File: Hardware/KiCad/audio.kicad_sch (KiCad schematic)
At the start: 36 parts, among them IC1 LM4861M, J4 Kenwood-3.5, J5 Kenwood-2.5, SW1 PTT, U5 MAX9814

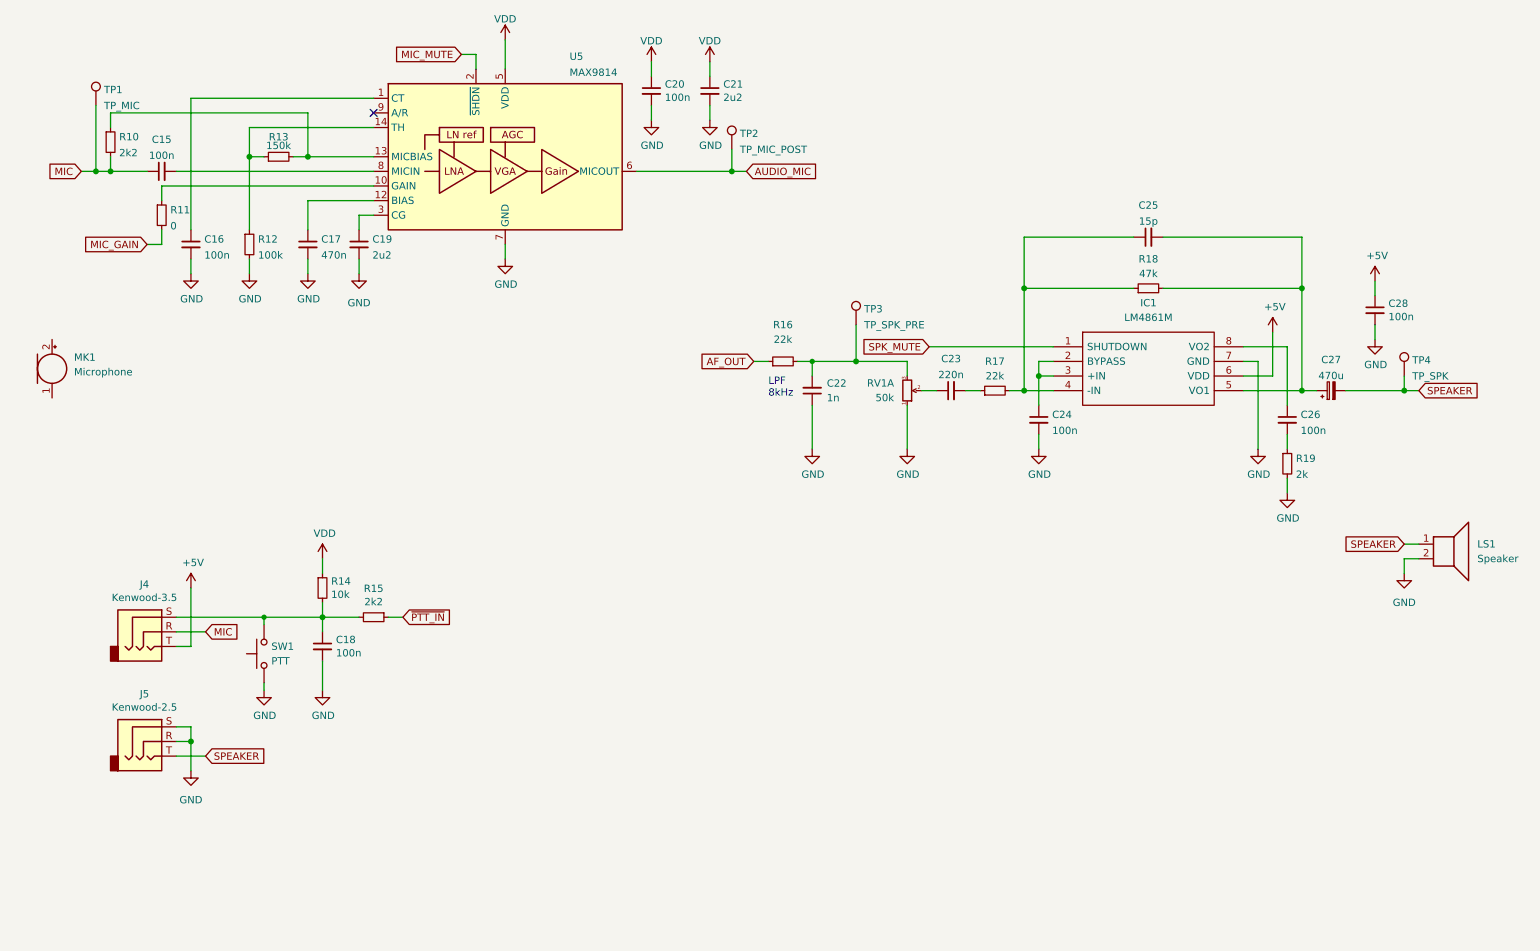
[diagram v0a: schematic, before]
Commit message: fixup PTT/Audio (Issue 14), add RGB LED (Issue 26), Connect LEDs to MCU & add them to the .ioc file
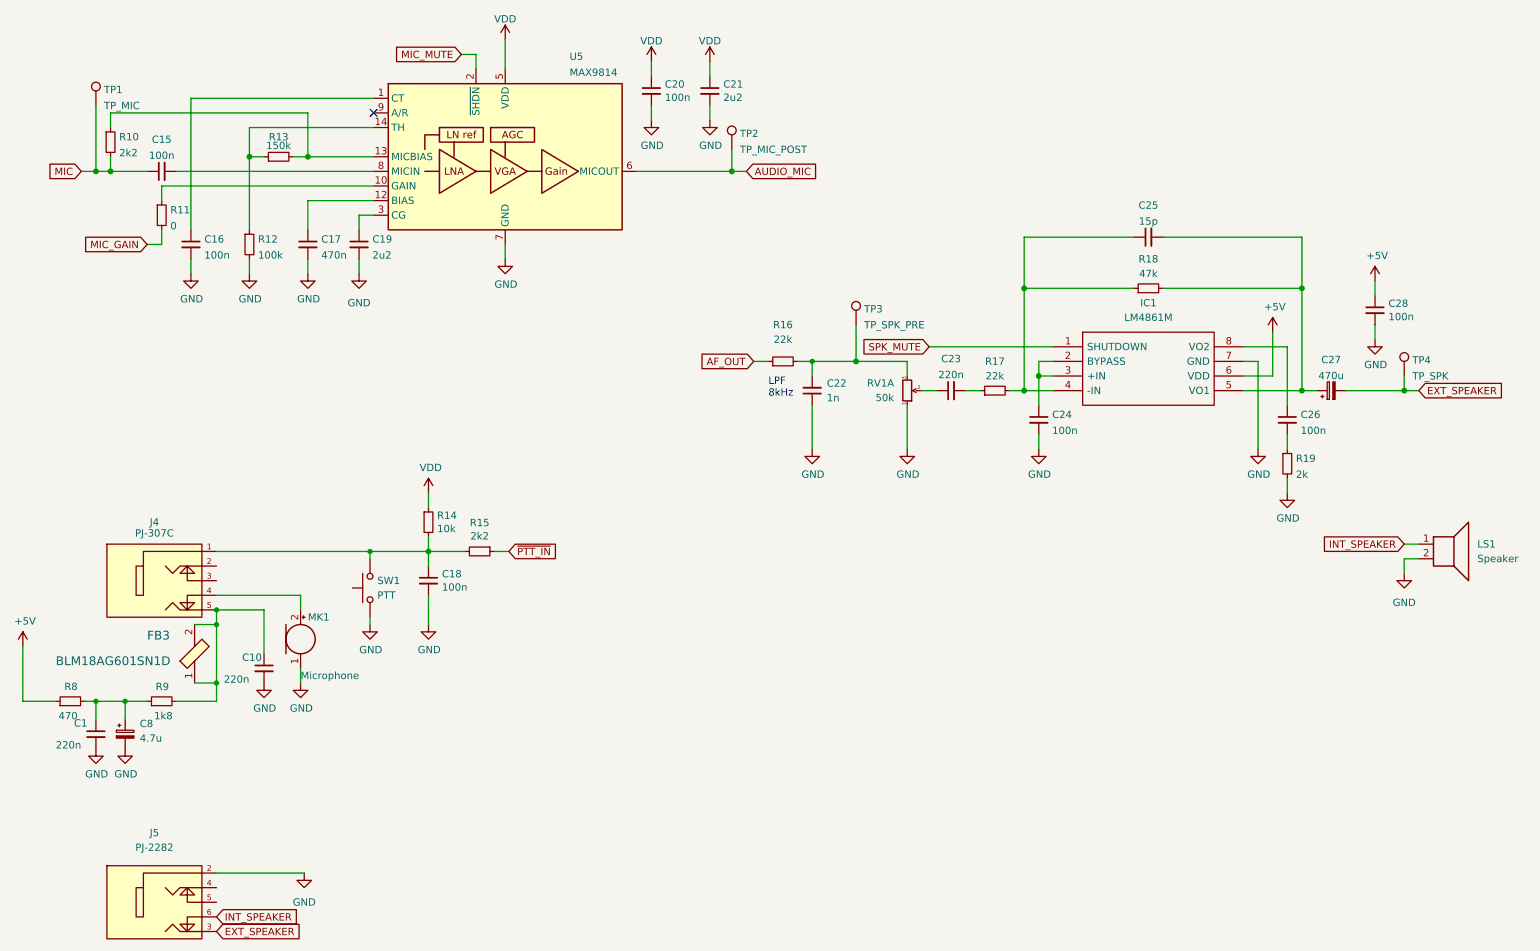
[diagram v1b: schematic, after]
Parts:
- removed J4: Kenwood-3.5, M17-SmartMic:PJ-3136-B, symbol Connector:AudioJack3
- removed J5: Kenwood-2.5, M17-SmartMic:PJ-211A, symbol Connector:AudioJack3
- added C1, C10: 220n, Capacitor_SMD:C_0402_1005Metric, symbol pkl_device:pkl_C_Small
- added C8: 4.7u, Capacitor_SMD:C_0402_1005Metric, symbol Device:C_Polarized_Small
- added FB3: BLM18AG601SN1D, digikey-footprints:0603, symbol dk_Ferrite-Beads-and-Chips:BLM18AG601SN1D
- added J4: PJ-307C, symbol AudioJack:PJ-307C
- added J5: PJ-2282, symbol AudioJack:PJ-2282
- added R8: 470, Resistor_SMD:R_0402_1005Metric, symbol pkl_device:pkl_R_Small
- added R9: 1k8, Resistor_SMD:R_0402_1005Metric, symbol pkl_device:pkl_R_Small
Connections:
- net +5V: now also R8.1
- net GND: now also MK1.1 (-), C1.2, C10.2, C8.2, J5.2
- net at C18.1, R14.2, R15.2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: now also J4.1
- net at MK1.2 (+): now also J4.4
- net SPEAKER renamed EXT_SPEAKER
- net EXT_SPEAKER: now also J5.3; no longer LS1.1
- new net: C10.1, FB3.1, FB3.2, J4.5, R9.2
- new net: C1.1, C8.1, R8.2, R9.1
- new net INT_SPEAKER: J5.6, LS1.1
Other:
- moved on the sheet: C18, MK1, R14, R15, SW1

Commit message: Minor corrections
- fixed microphone connection and part values
- added a few TPs
- changed C27 footprint
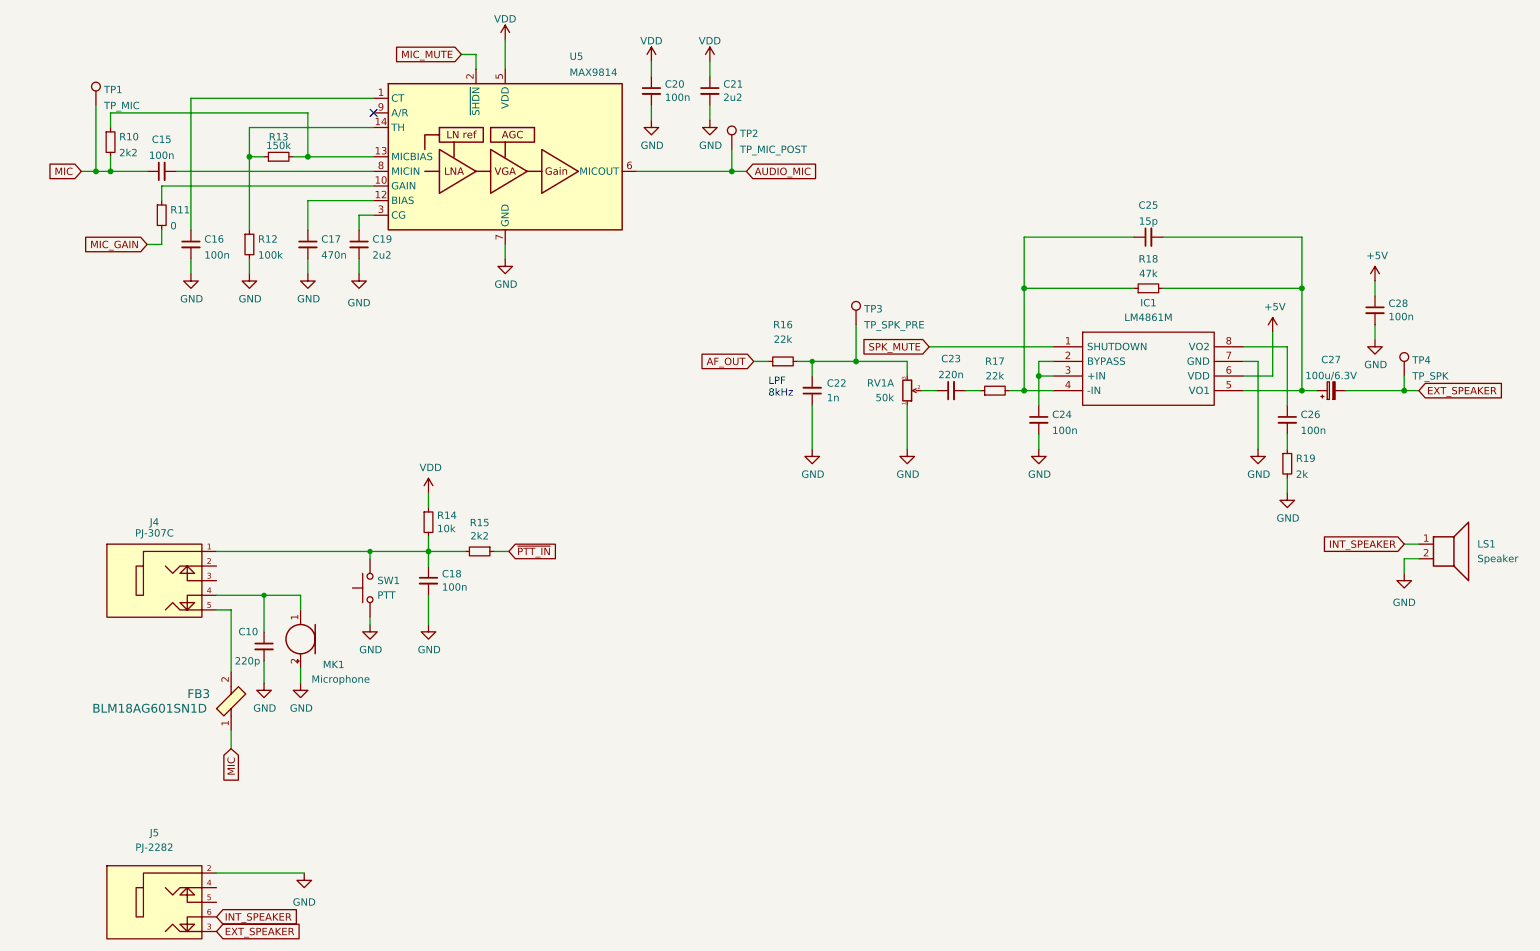
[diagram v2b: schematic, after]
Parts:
- removed C1: 220n, Capacitor_SMD:C_0402_1005Metric, symbol pkl_device:pkl_C_Small
- removed C8: 4.7u, Capacitor_SMD:C_0402_1005Metric, symbol Device:C_Polarized_Small
- removed R8: 470, Resistor_SMD:R_0402_1005Metric, symbol pkl_device:pkl_R_Small
- removed R9: 1k8, Resistor_SMD:R_0402_1005Metric, symbol pkl_device:pkl_R_Small
- C10: value 220n -> 220p
- C27: value 470u -> 100u/6.3V; footprint Capacitor_SMD:CP_Elec_6.3x7.7 -> Capacitor_SMD:C_1206_3216Metric
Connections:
- net GND: now also MK1.2 (+); no longer MK1.1 (-)
- net MIC: now also FB3.1
- net at FB3.2, J4.5: no longer C10.1, FB3.1
- net at J4.4: now also C10.1, MK1.1 (-); no longer MK1.2 (+)
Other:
- moved on the sheet: C10, MK1
